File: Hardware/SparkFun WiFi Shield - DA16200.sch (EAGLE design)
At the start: 33 parts, among them J1 CORTEX_JTAG_DEBUG, J4 QWIIC_RA, U1 DA16200MOD

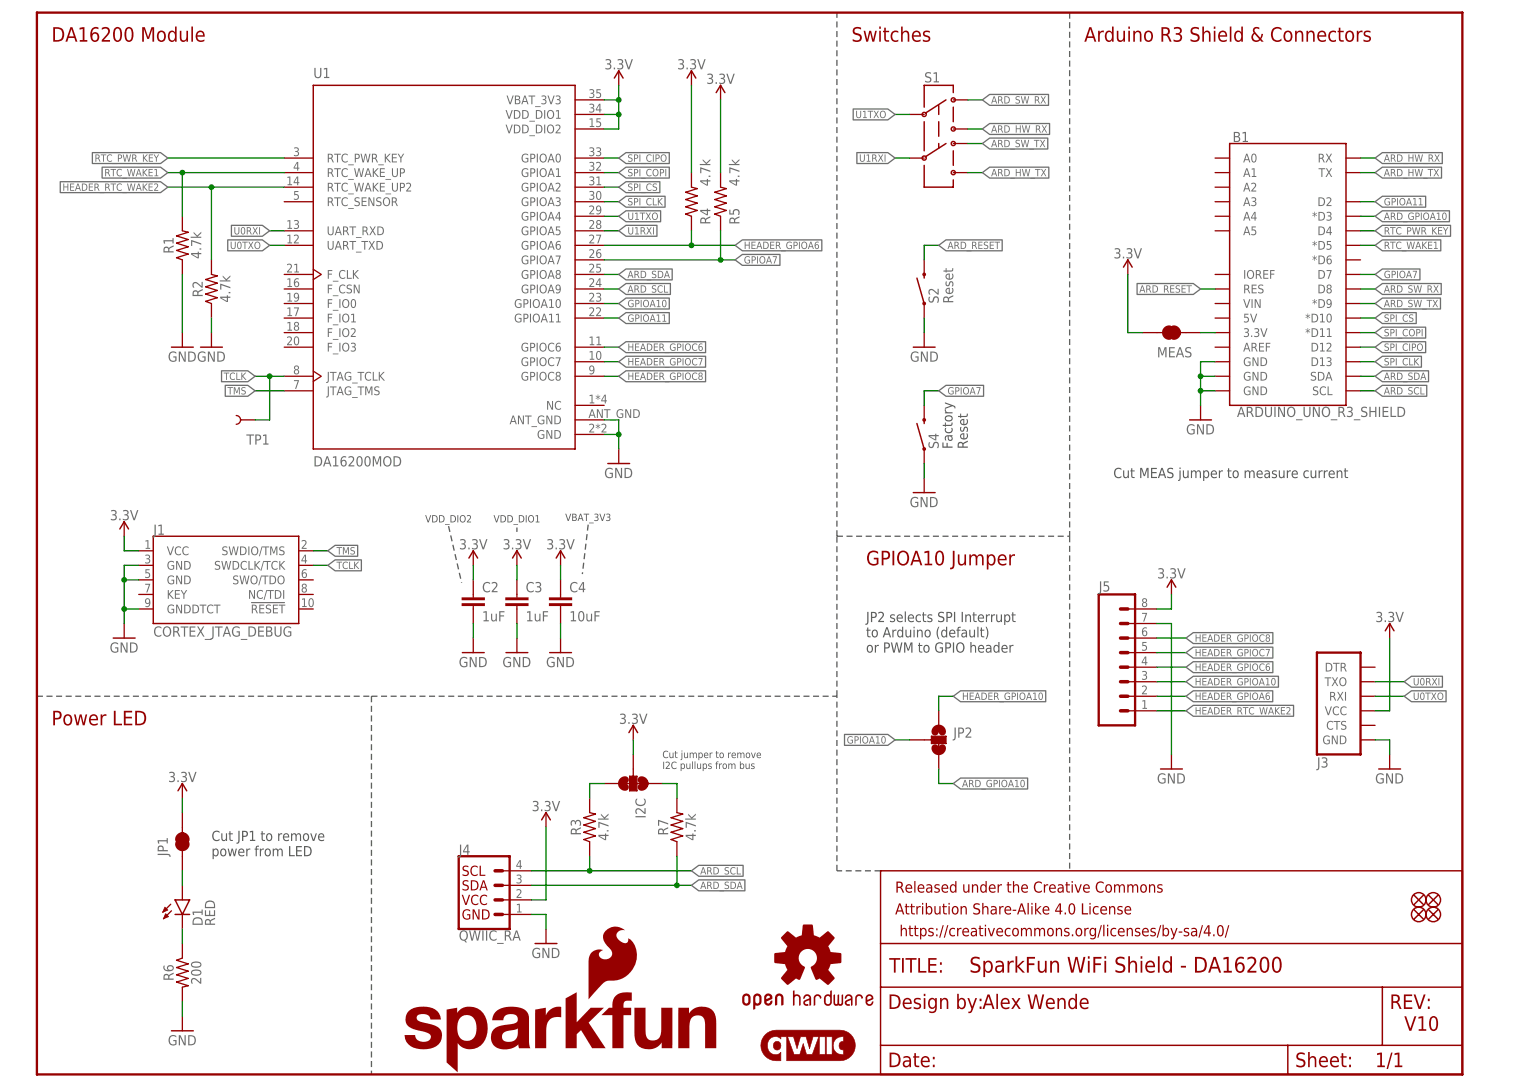
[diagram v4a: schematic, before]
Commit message: Final Feedback Changes
Changed R3 footprint to locking
Added DNP Capacitor and Resistor
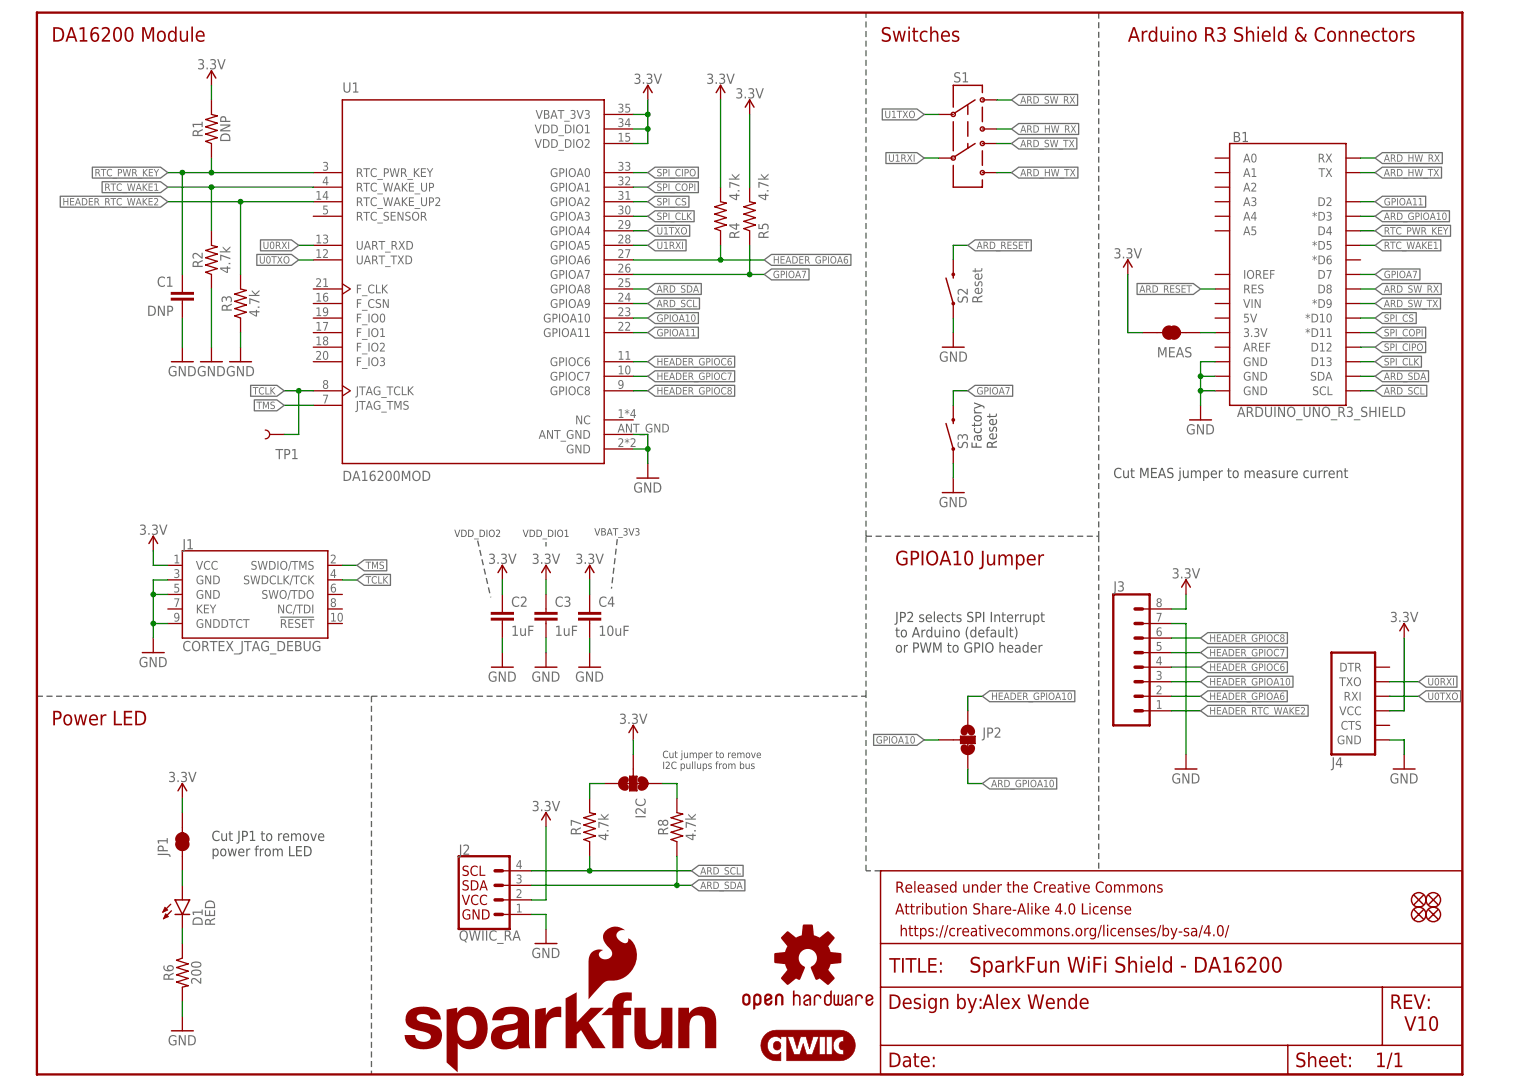
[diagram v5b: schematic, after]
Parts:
- removed J5: (no value), SparkFun-Connectors:CONN_08NO_SILK_DNP
- removed S4: MOMENTARY-SWITCH-SPST-SMD-5.2MM-TALL, SparkFun-Switches:MOMENTARY-SWITCH-SPST-SMD-5.2MM-TALL
- added C1: DNP, SparkFun-Capacitors:CAP-0603
- added J2: QWIIC_RA, SparkFun-Connectors:QWIIC_CONNECTORJS-1MM
- added R8: 4.7k, SparkFun-Resistors:4.7KOHM-0603-1/10W-1%
- added S3: MOMENTARY-SWITCH-SPST-SMD-5.2MM-TALL, SparkFun-Switches:MOMENTARY-SWITCH-SPST-SMD-5.2MM-TALL
- B1: device SparkFun-Boards:ARDUINO_UNO_R3_SHIELDNOLABELS -> SparkFun-Boards:ARDUINO_UNO_R3_SHIELDUNO_R3_SHIELD_NOLABELS_LOCK
- J3: device SparkFun-Connectors:6_PIN_SERIAL_TARGET_NO_SILK -> SparkFun-Connectors:CONN_08NO_SILK_DNP
- J4: value QWIIC_RA -> (none); device SparkFun-Connectors:QWIIC_CONNECTORJS-1MM -> SparkFun-Connectors:6_PIN_SERIAL_TARGET_NO_SILK
- R1: value 4.7k -> DNP; device SparkFun-Resistors:4.7KOHM-0603-1/10W-1% -> SparkFun-Resistors:RESISTOR0603
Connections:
- net 3.3V: now also J2.2, J3.8, J4.VCC, R1.2; no longer J3.VCC, J4.2, J5.8
- net ARD_SCL: now also J2.4, R7.1; no longer J4.4, R3.1
- net ARD_SDA: now also J2.3, R8.1; no longer J4.3, R7.1
- net GND: now also C1.2, J2.1, J3.7, J4.GND, R3.1, S3.1; no longer J3.GND, J4.1, J5.7, R1.1, S4.1
- net GPIOA7: now also S3.2; no longer S4.2
- net HEADER_GPIOA10: now also J3.3; no longer J5.3
- net HEADER_GPIOA6: now also J3.2; no longer J5.2
- net HEADER_GPIOC6: now also J3.4; no longer J5.4
- net HEADER_GPIOC7: now also J3.5; no longer J5.5
- net HEADER_GPIOC8: now also J3.6; no longer J5.6
- net HEADER_RTC_WAKE2: now also J3.1, R3.2; no longer J5.1, R2.2
- net N$3: now also R7.2; no longer R3.2
- net N$4: now also R8.2; no longer R7.2
- net RTC_PWR_KEY: now also C1.1, R1.1
- net RTC_WAKE1: now also R2.2; no longer R1.2
- net U0RXI: now also J4.TXO; no longer J3.TXO
- net U0TXO: now also J4.RXI; no longer J3.RXI
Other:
- moved on the sheet: C2, C3, C4, J1, JP2, R1, R2, R3, R4, R5, R7, S1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

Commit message: Added jumpers for GPIOA0-3
Jumpers select between either SPI or GPIO/ADC functionality on the DA16200
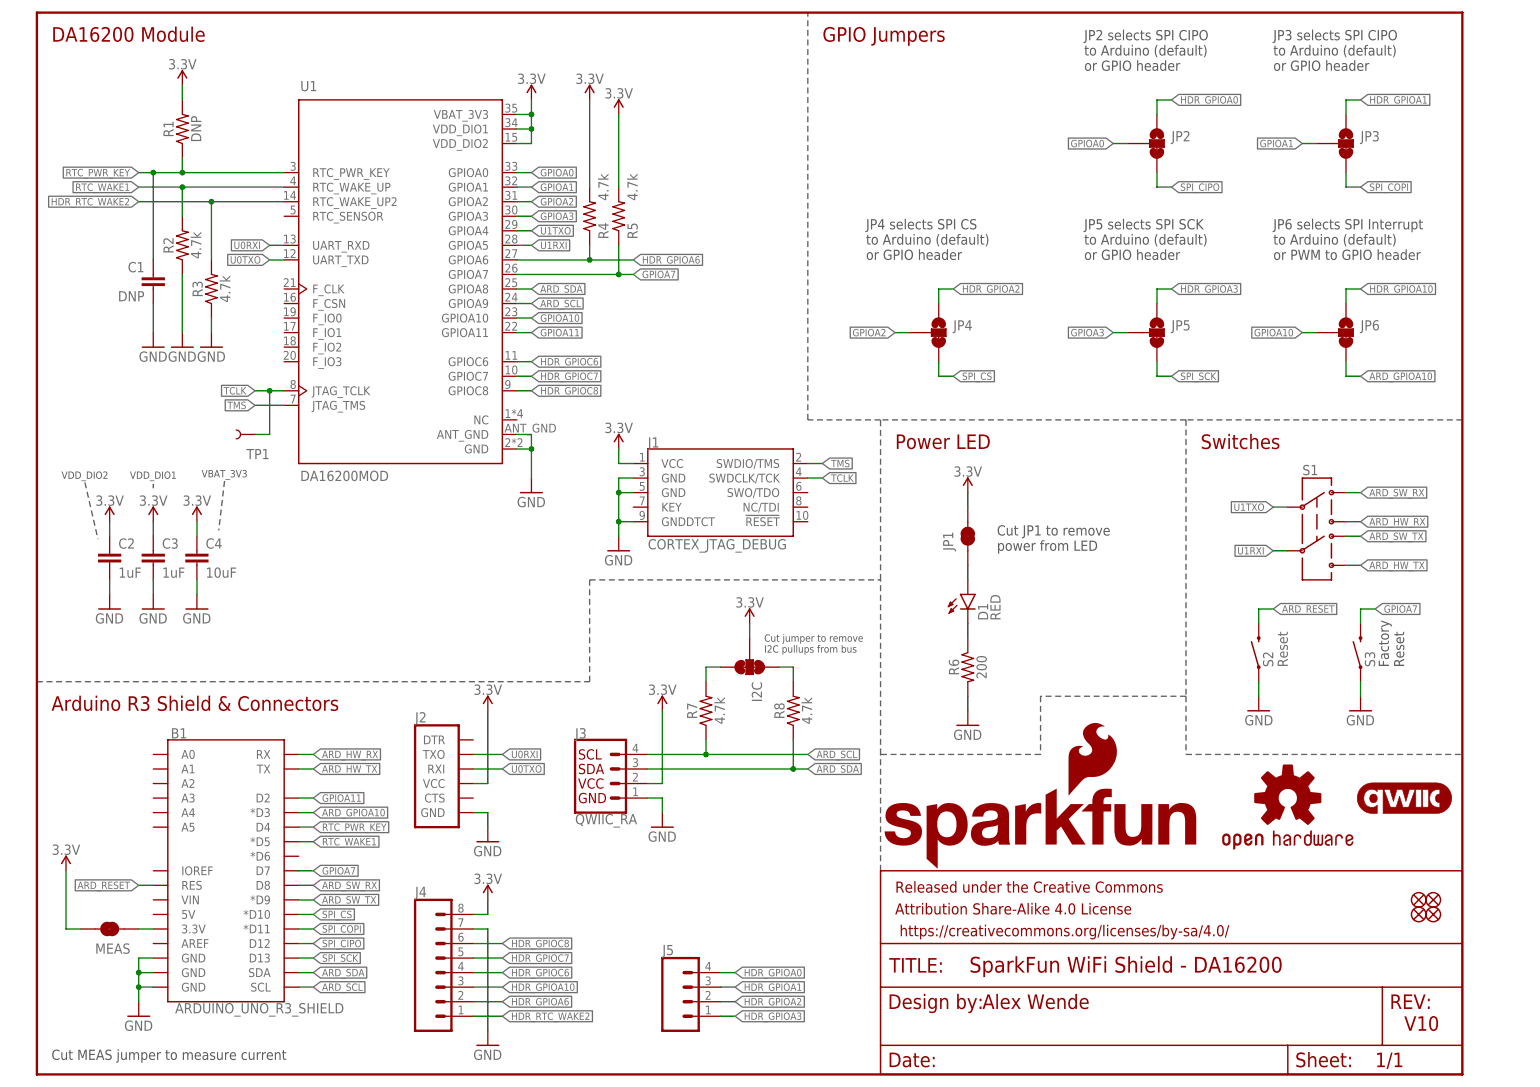
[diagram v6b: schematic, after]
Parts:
- added J5: (no value), SparkFun-Connectors:CONN_041X04_NO_SILK
- added JP3, JP4, JP5, JP6: JUMPER-SMT_3_1-NC_TRACE_SILK, SparkFun-Jumpers:JUMPER-SMT_3_1-NC_TRACE_SILK
- J2: value QWIIC_RA -> (none); device SparkFun-Connectors:QWIIC_CONNECTORJS-1MM -> SparkFun-Connectors:6_PIN_SERIAL_TARGET_NO_SILK
- J3: value (none) -> QWIIC_RA; device SparkFun-Connectors:CONN_08NO_SILK_DNP -> SparkFun-Connectors:QWIIC_CONNECTORJS-1MM
- J4: device SparkFun-Connectors:6_PIN_SERIAL_TARGET_NO_SILK -> SparkFun-Connectors:CONN_08NO_SILK_DNP
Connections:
- removed net HEADER_GPIOA10: J3.3, JP2.1
- removed net HEADER_GPIOA6: J3.2, R4.1, U1.GPIOA6
- removed net HEADER_GPIOC6: J3.4, U1.GPIOC6
- removed net HEADER_GPIOC7: J3.5, U1.GPIOC7
- removed net HEADER_GPIOC8: J3.6, U1.GPIOC8
- removed net HEADER_RTC_WAKE2: J3.1, R3.2, U1.RTC_WAKE_UP2
- removed net SPI_CLK: B1.D13, U1.GPIOA3
- new net GPIOA0: JP2.2, U1.GPIOA0
- new net GPIOA1: JP3.2, U1.GPIOA1
- new net GPIOA2: JP4.2, U1.GPIOA2
- new net GPIOA3: JP5.2, U1.GPIOA3
- new net HDR_GPIOA0: J5.4, JP2.1
- new net HDR_GPIOA1: J5.3, JP3.1
- new net HDR_GPIOA10: J4.3, JP6.1
- new net HDR_GPIOA2: J5.2, JP4.1
- new net HDR_GPIOA3: J5.1, JP5.1
- new net HDR_GPIOA6: J4.2, R4.1, U1.GPIOA6
- new net HDR_GPIOC6: J4.4, U1.GPIOC6
- new net HDR_GPIOC7: J4.5, U1.GPIOC7
- new net HDR_GPIOC8: J4.6, U1.GPIOC8
- new net HDR_RTC_WAKE2: J4.1, R3.2, U1.RTC_WAKE_UP2
- new net SPI_SCK: B1.D13, JP5.3
- net 3.3V: now also J2.VCC, J3.2, J4.8; no longer J2.2, J3.8, J4.VCC
- net ARD_GPIOA10: now also JP6.3; no longer JP2.3
- net ARD_SCL: now also J3.4; no longer J2.4
- net ARD_SDA: now also J3.3; no longer J2.3
- net GND: now also J2.GND, J3.1, J4.7; no longer J2.1, J3.7, J4.GND
- net GPIOA10: now also JP6.2; no longer JP2.2
- net SPI_CIPO: now also JP2.3; no longer U1.GPIOA0
- net SPI_COPI: now also JP3.3; no longer U1.GPIOA1
- net SPI_CS: now also JP4.3; no longer U1.GPIOA2
- net U0RXI: now also J2.TXO; no longer J4.TXO
- net U0TXO: now also J2.RXI; no longer J4.RXI
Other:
- note added: "GPIO Jumpers"
- note added: "JP2 selects SPI CIPO to Arduino (default) or GPIO header"
- note added: "JP3 selects SPI CIPO to Arduino (default) or GPIO header"
- note added: "JP4 selects SPI CS to Arduino (default) or GPIO header"
- note added: "JP5 selects SPI SCK to Arduino (default) or GPIO header"
- note added: "JP6 selects SPI Interrupt to Arduino (default) or PWM to GPIO header"
- note removed: "GPIOA10 Jumper"
- note removed: "JP2 selects SPI Interrupt to Arduino (default) or PWM to GPIO header"
- moved on the sheet: B1, C1, C2, C3, C4, D1, I2C, J1, JP1, JP2, MEAS, R1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

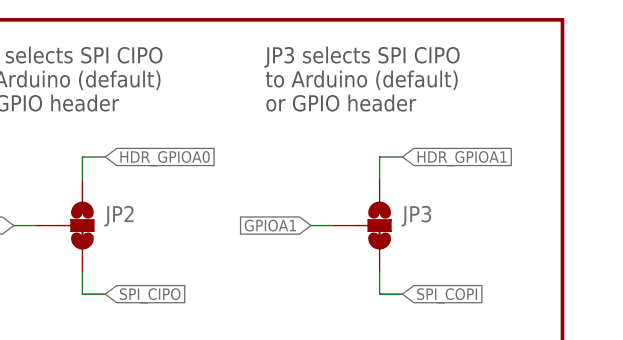
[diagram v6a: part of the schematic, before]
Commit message: Update SparkFun WiFi Shield - DA16200.sch
Fixed typo for JP3
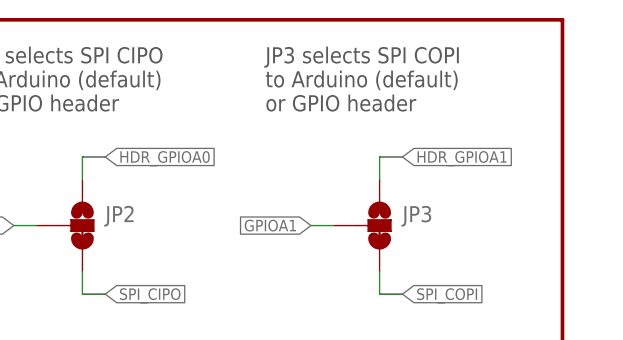
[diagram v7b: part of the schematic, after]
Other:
- note added: "JP3 selects SPI COPI to Arduino (default) or GPIO header"
- note removed: "JP3 selects SPI CIPO to Arduino (default) or GPIO header"
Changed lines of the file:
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@@
 to Arduino (default)
 or GPIO header</text>
-<text x="215.9" y="175.26" size="1.778" layer="97" font="vector">JP3 selects SPI CIPO
+<text x="215.9" y="175.26" size="1.778" layer="97" font="vector">JP3 selects SPI COPI
 to Arduino (default)
 or GPIO header</text>
